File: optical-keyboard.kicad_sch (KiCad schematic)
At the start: 22 parts, among them U1 BlackPill_STLINK

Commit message: updated pcb
M  optical-keyboard.kicad_pcb
M  optical-keyboard.kicad_pro
M  optical-keyboard.kicad_sch
M  placefp.py
M  switch.kicad_sch
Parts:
- added H?: MountingHole, OpticalParts:MountingHole_2.2mm_M2_jlcpcb, symbol Mechanical:MountingHole
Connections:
- net GND: no longer U1.44 (GND)
- no-connect marks 19 -> 20
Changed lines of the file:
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@@
   (junction (at 194.31 92.71) (diameter 0) (color 0 0 0 0)
   )
-  (junction (at 241.3 90.17) (diameter 0) (color 0 0 0 0)
-  )
   (junction (at 77.47 160.02) (diameter 0) (color 0 0 0 0)
   )
@@
   (no_connect (at 228.6 64.77))
   (no_connect (at 236.22 29.21))
+  (no_connect (at 243.84 87.63))
   (no_connect (at 254 78.74))
   (no_connect (at 254 44.45))
@@
     (stroke (width 0) (type default) (color 0 0 0 0))
   )
-  (wire (pts (xy 243.84 87.63) (xy 243.84 90.17))
-    (stroke (width 0) (type default) (color 0 0 0 0))
-  )
   (wire (pts (xy 66.04 160.02) (xy 66.04 153.67))
     (stroke (width 0) (type default) (color 0 0 0 0))
@@
     (stroke (width 0) (type default) (color 0 0 0 0))
   )
-  (wire (pts (xy 243.84 90.17) (xy 241.3 90.17))
-    (stroke (width 0) (type default) (color 0 0 0 0))
-  )
   (wire (pts (xy 135.89 160.02) (xy 124.46 160.02))
     (stroke (width 0) (type default) (color 0 0 0 0))
@@
     )
   )
+  (symbol (lib_id "Mechanical:MountingHole") (at 137.16 176.53 0) (unit 1)
+    (in_bom yes) (on_board yes) (fields_autoplaced)
+    (property "Reference" "H?" (id 0) (at 139.7 175.6953 0)
+      (effects (font (size 1.27 1.27)) (justify left))
+    )
+    (property "Value" "MountingHole" (id 1) (at 139.7 178.2322 0)
+      (effects (font (size 1.27 1.27)) (justify left))
+    )
+    (property "Footprint" "OpticalParts:MountingHole_2.2mm_M2_jlcpcb" (id 2) (at 137.16 176.53 0)
+      (effects (font (size 1.27 1.27)) hide)
+    )
+    (property "Datasheet" "~" (id 3) (at 137.16 176.53 0)
+      (effects (font (size 1.27 1.27)) hide)
+    )
+  )
   (symbol (lib_id "Mechanical:MountingHole") (at 68.58 176.53 0) (unit 1)
     (in_bom yes) (on_board yes) (fields_autoplaced)
@@
       (reference "H19") (unit 1) (value "MountingHole") (footprint "OpticalParts:TestPoint_Plated_Hole_D1.2mm")
     )
+    (path "/a466dee4-f4c6-4564-b0e5-4beb0c27276a"
+      (reference "H?") (unit 1) (value "MountingHole") (footprint "OpticalParts:MountingHole_2.2mm_M2_jlcpcb")
+    )
     (path "/23d7508b-7c29-44fb-a276-a12f2a3d1508/86f62c6e-cc97-4257-bd64-06b736e80ca7"

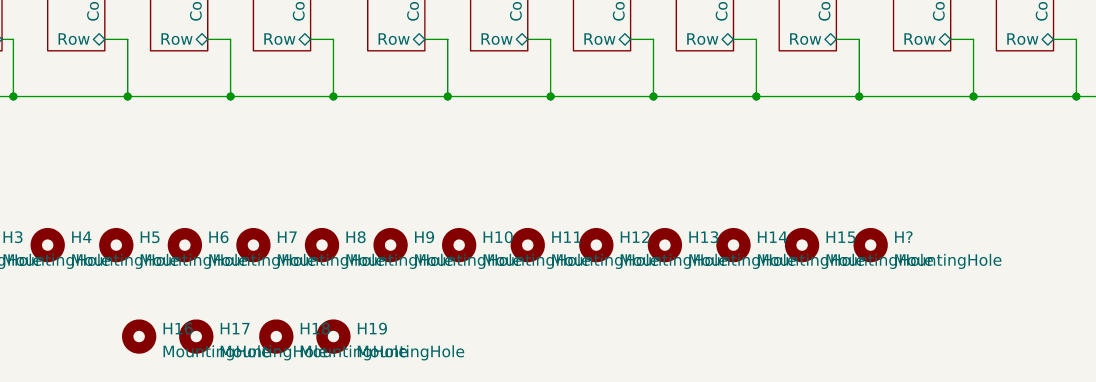
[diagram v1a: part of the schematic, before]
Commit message: update schematic
M  optical-keyboard.kicad_sch
M  switch.kicad_sch
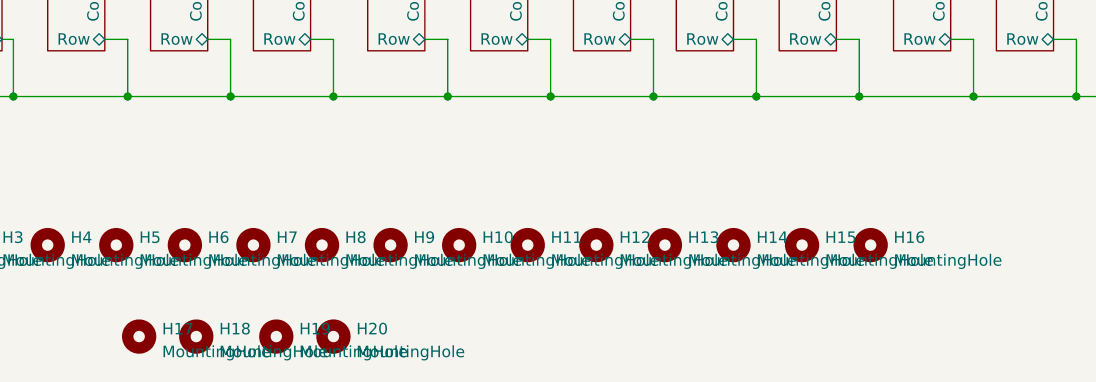
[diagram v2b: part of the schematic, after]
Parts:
- gave numbers to parts that had none: 1
- renumbered H16 to H17, H17 to H18, H18 to H19, H19 to H20
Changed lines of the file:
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@@
   (symbol (lib_id "Mechanical:MountingHole") (at 55.88 186.69 0) (unit 1)
     (in_bom yes) (on_board yes) (fields_autoplaced)
-    (property "Reference" "H16" (id 0) (at 58.42 185.8553 0)
+    (property "Reference" "H17" (id 0) (at 58.42 185.8553 0)
       (effects (font (size 1.27 1.27)) (justify left))
     )
@@
   (symbol (lib_id "Mechanical:MountingHole") (at 62.23 186.69 0) (unit 1)
     (in_bom yes) (on_board yes) (fields_autoplaced)
-    (property "Reference" "H17" (id 0) (at 64.77 185.8553 0)
+    (property "Reference" "H18" (id 0) (at 64.77 185.8553 0)
       (effects (font (size 1.27 1.27)) (justify left))
     )
@@
   (symbol (lib_id "Mechanical:MountingHole") (at 71.12 186.69 0) (unit 1)
     (in_bom yes) (on_board yes) (fields_autoplaced)
-    (property "Reference" "H18" (id 0) (at 73.66 185.8553 0)
+    (property "Reference" "H19" (id 0) (at 73.66 185.8553 0)
       (effects (font (size 1.27 1.27)) (justify left))
     )
@@
   (symbol (lib_id "Mechanical:MountingHole") (at 77.47 186.69 0) (unit 1)
     (in_bom yes) (on_board yes) (fields_autoplaced)
-    (property "Reference" "H19" (id 0) (at 80.01 185.8553 0)
+    (property "Reference" "H20" (id 0) (at 80.01 185.8553 0)
       (effects (font (size 1.27 1.27)) (justify left))
     )
@@
   (symbol (lib_id "Mechanical:MountingHole") (at 137.16 176.53 0) (unit 1)
     (in_bom yes) (on_board yes) (fields_autoplaced)
-    (property "Reference" "H?" (id 0) (at 139.7 175.6953 0)
+    (property "Reference" "H16" (id 0) (at 139.7 175.6953 0)
       (effects (font (size 1.27 1.27)) (justify left))
     )
@@
       (reference "H15") (unit 1) (value "MountingHole") (footprint "OpticalParts:MountingHole_2.2mm_M2_jlcpcb")
     )
+    (path "/a466dee4-f4c6-4564-b0e5-4beb0c27276a"
+      (reference "H16") (unit 1) (value "MountingHole") (footprint "OpticalParts:MountingHole_2.2mm_M2_jlcpcb")
+    )
     (path "/1c5e075c-0d59-4f41-b288-1d43e8849604"
-      (reference "H16") (unit 1) (value "MountingHole") (footprint "OpticalParts:TestPoint_Plated_Hole_D1.2mm")
+      (reference "H17") (unit 1) (value "MountingHole") (footprint "OpticalParts:TestPoint_Plated_Hole_D1.2mm")
     )
     (path "/4a6dd189-df51-490b-973b-801cd824fa41"
-      (reference "H17") (unit 1) (value "MountingHole") (footprint "OpticalParts:TestPoint_Plated_Hole_D1.2mm")
+      (reference "H18") (unit 1) (value "MountingHole") (footprint "OpticalParts:TestPoint_Plated_Hole_D1.2mm")
     )
     (path "/4f3af77f-a4c8-4cfb-b814-08fdd220c175"
-      (reference "H18") (unit 1) (value "MountingHole") (footprint "OpticalParts:TestPoint_Plated_Hole_D1.2mm")
+      (reference "H19") (unit 1) (value "MountingHole") (footprint "OpticalParts:TestPoint_Plated_Hole_D1.2mm")
     )
     (path "/5c35b6b4-665e-49cb-b198-1d19488004f2"
-      (reference "H19") (unit 1) (value "MountingHole") (footprint "OpticalParts:TestPoint_Plated_Hole_D1.2mm")
-    )
-    (path "/a466dee4-f4c6-4564-b0e5-4beb0c27276a"
-      (reference "H?") (unit 1) (value "MountingHole") (footprint "OpticalParts:MountingHole_2.2mm_M2_jlcpcb")
+      (reference "H20") (unit 1) (value "MountingHole") (footprint "OpticalParts:TestPoint_Plated_Hole_D1.2mm")
     )
     (path "/23d7508b-7c29-44fb-a276-a12f2a3d1508/86f62c6e-cc97-4257-bd64-06b736e80ca7"

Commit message: Fixed bug in symbols by removing arrows
M  optical-keyboard.kicad_sch
M  switch.kicad_sch
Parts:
- U1: footprint OpticalParts:BlackPill_STLINK2 -> blackpill:BlackPill_STLINK

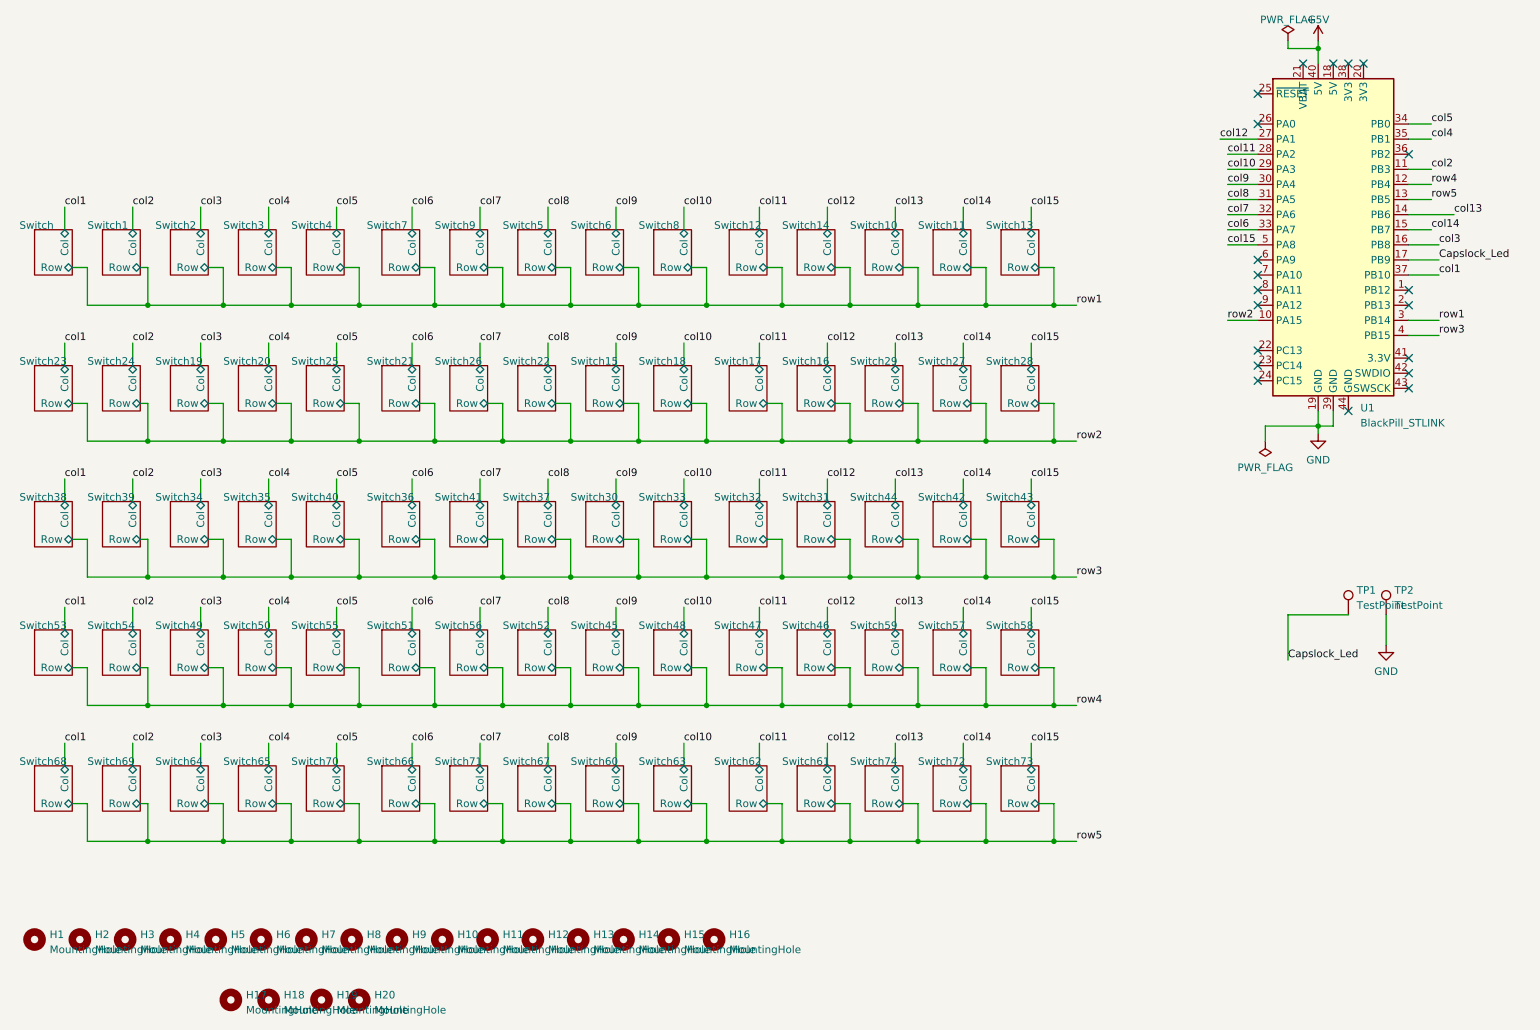
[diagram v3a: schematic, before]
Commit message: Add separate power source for PTs
Sharing input pin b/w pt and led requires a diode, and diode
slows down the response time of pt considerably

M  optical-keyboard.kicad_pcb
M  optical-keyboard.kicad_prl
M  optical-keyboard.kicad_sch
M  placefp.py
M  switch.kicad_sch
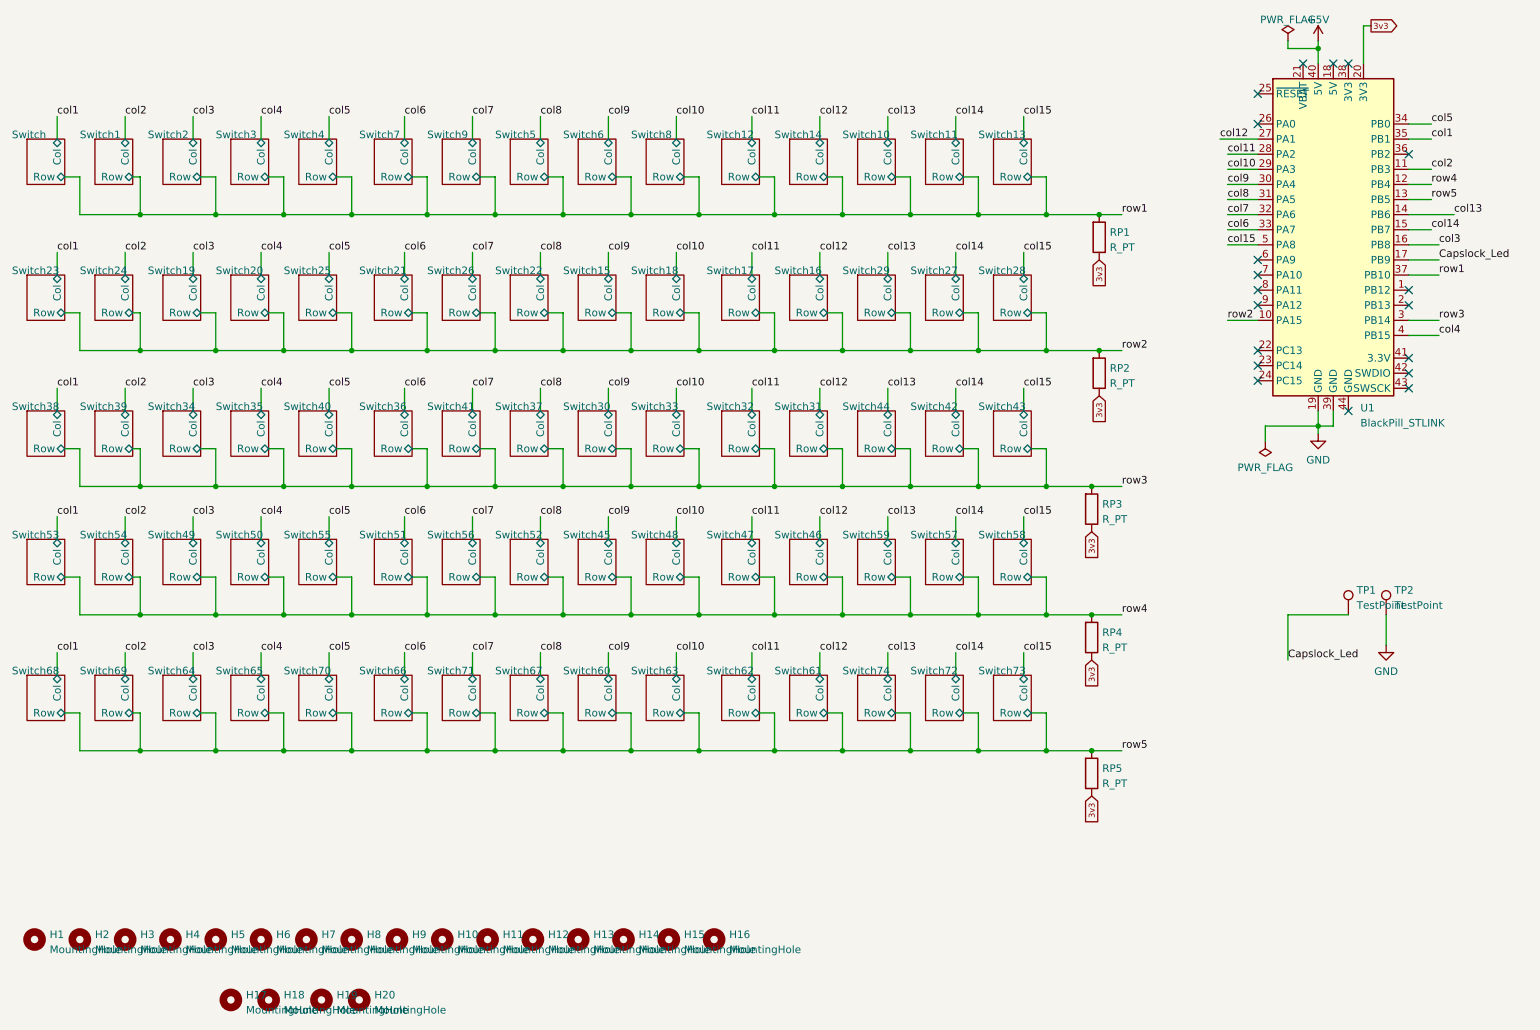
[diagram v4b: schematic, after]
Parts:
- added RP1, RP2, RP3, RP4, RP5: R_PT, Resistor_SMD:R_0805_2012Metric, symbol OpticalParts:R_PT
- U1: footprint blackpill:BlackPill_STLINK -> OpticalParts:BlackPill_STLINK2
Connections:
- net col1: now also U1.35 (PB1); no longer U1.37 (PB10)
- net col4: now also U1.4 (PB15); no longer U1.35 (PB1)
- net row1: now also U1.37 (PB10), RP1.1; no longer U1.3 (PB14)
- net row2: now also RP2.1
- net row3: now also U1.3 (PB14), RP3.1; no longer U1.4 (PB15)
- net row4: now also RP4.1
- net row5: now also RP5.1
- net 3v3: now reaches U1.20 (3V3)
- net 3v3: now also RP1.2, RP2.2, RP3.2, RP4.2, RP5.2
- no-connect marks 20 -> 19
